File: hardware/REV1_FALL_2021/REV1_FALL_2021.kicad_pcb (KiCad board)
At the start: 2 copper layers, 146 x 133.4 mm, 38 parts, among them J101 Screw_Terminal_01x02, J102 Screw_Terminal_01x02, Q101 Q_NMOS_GDS, Q102 Q_NMOS_GDS, U1 Teensy3.6_All_Pins, U2 PA16165_Breakout, U201 TPS2113ADRBR, U3 MPL3115A2_Breakout, U301 TPS2113ADRBR, U4 BNO055_Breakout, U5 RFM69HCW_Breakout

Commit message: add logos and authors
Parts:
- added G***: LOGO, Olin_Rocketry:Olin_O, B.Cu at (97.9, 74.9)
- added G***: LOGO, Olin_Rocketry:Olin_Rocketry_Logo1, B.Cu at (100.2, 114.9)
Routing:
- net /E-MATCH_TRIGGER_2: track 0.00 -> 39.7 mm, vias 0 -> 1
- net GND: track 981.1 -> 982.8 mm
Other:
- board text added: "Ian Eykamp Marc Eftimie Charlie Babe Nov. 24, 2021 Pheonix IV Rev. 1"

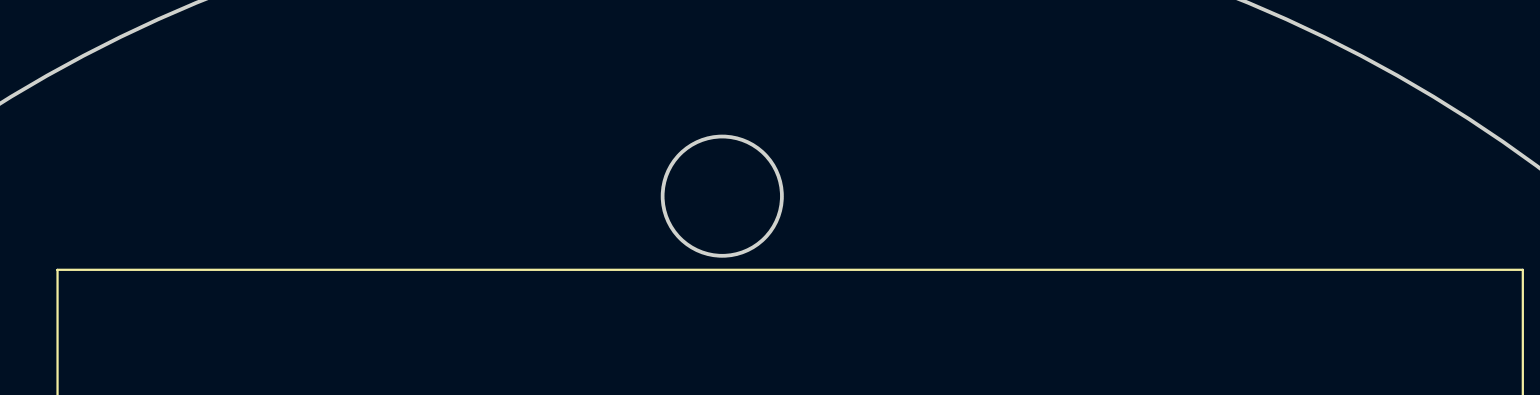
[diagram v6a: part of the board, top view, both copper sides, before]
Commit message: add positive and negative signs on battery terminals
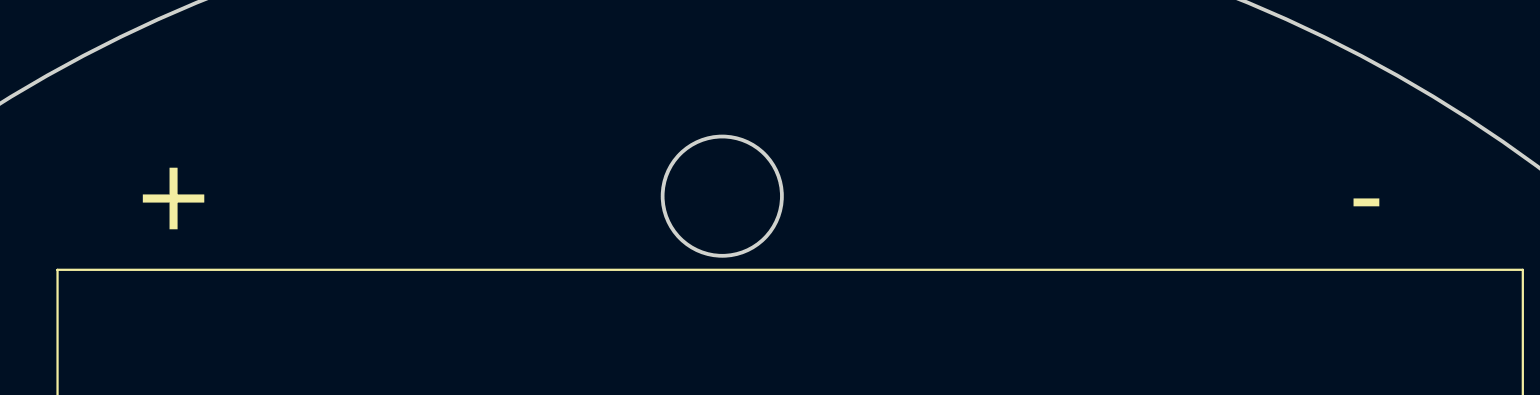
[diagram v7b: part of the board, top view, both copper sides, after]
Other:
- board text added: "+"
- board text added: "-"
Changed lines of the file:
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@@
   (general
     (thickness 1.6)
-    (drawings 6)
+    (drawings 8)
     (tracks 685)
     (zones 0)
@@
       (xy -13.7383 11.823811) (xy -13.641607 11.834288) (xy -13.637075 11.82514)) (layer B.SilkS) (width 0.01))
   )
+  (gr_text - (at 134.62 45.72) (layer F.SilkS)
+    (effects (font (size 3.81 3.81) (thickness 0.3)))
+  )
+  (gr_text + (at 71.12 45.72) (layer F.SilkS)
+    (effects (font (size 3.81 3.81) (thickness 0.3)))
+  )
   (gr_text "Ian Eykamp\nMarc Eftimie\nCharlie Babe\n\nNov. 24, 2021\nPheonix IV\nRev. 1" (at 129.286 145.923) (layer B.SilkS)

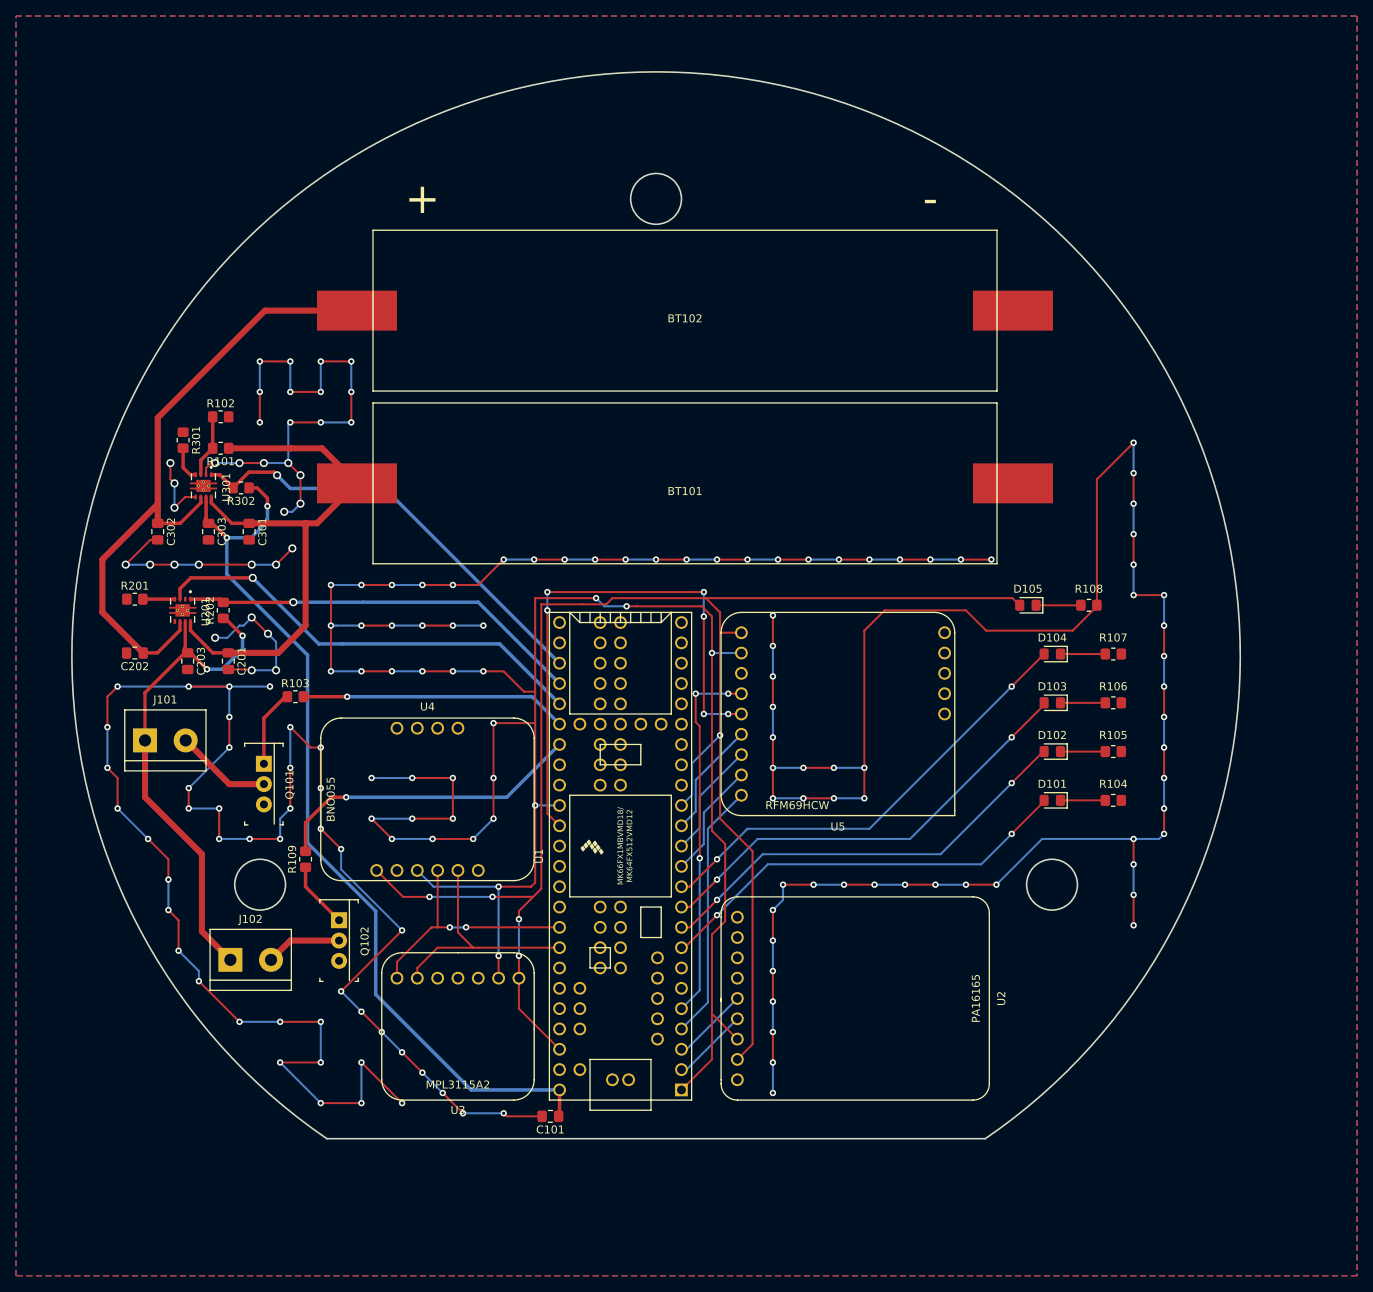
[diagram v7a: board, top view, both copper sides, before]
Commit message: Change footprint of TPS2113A to the TSSOP package
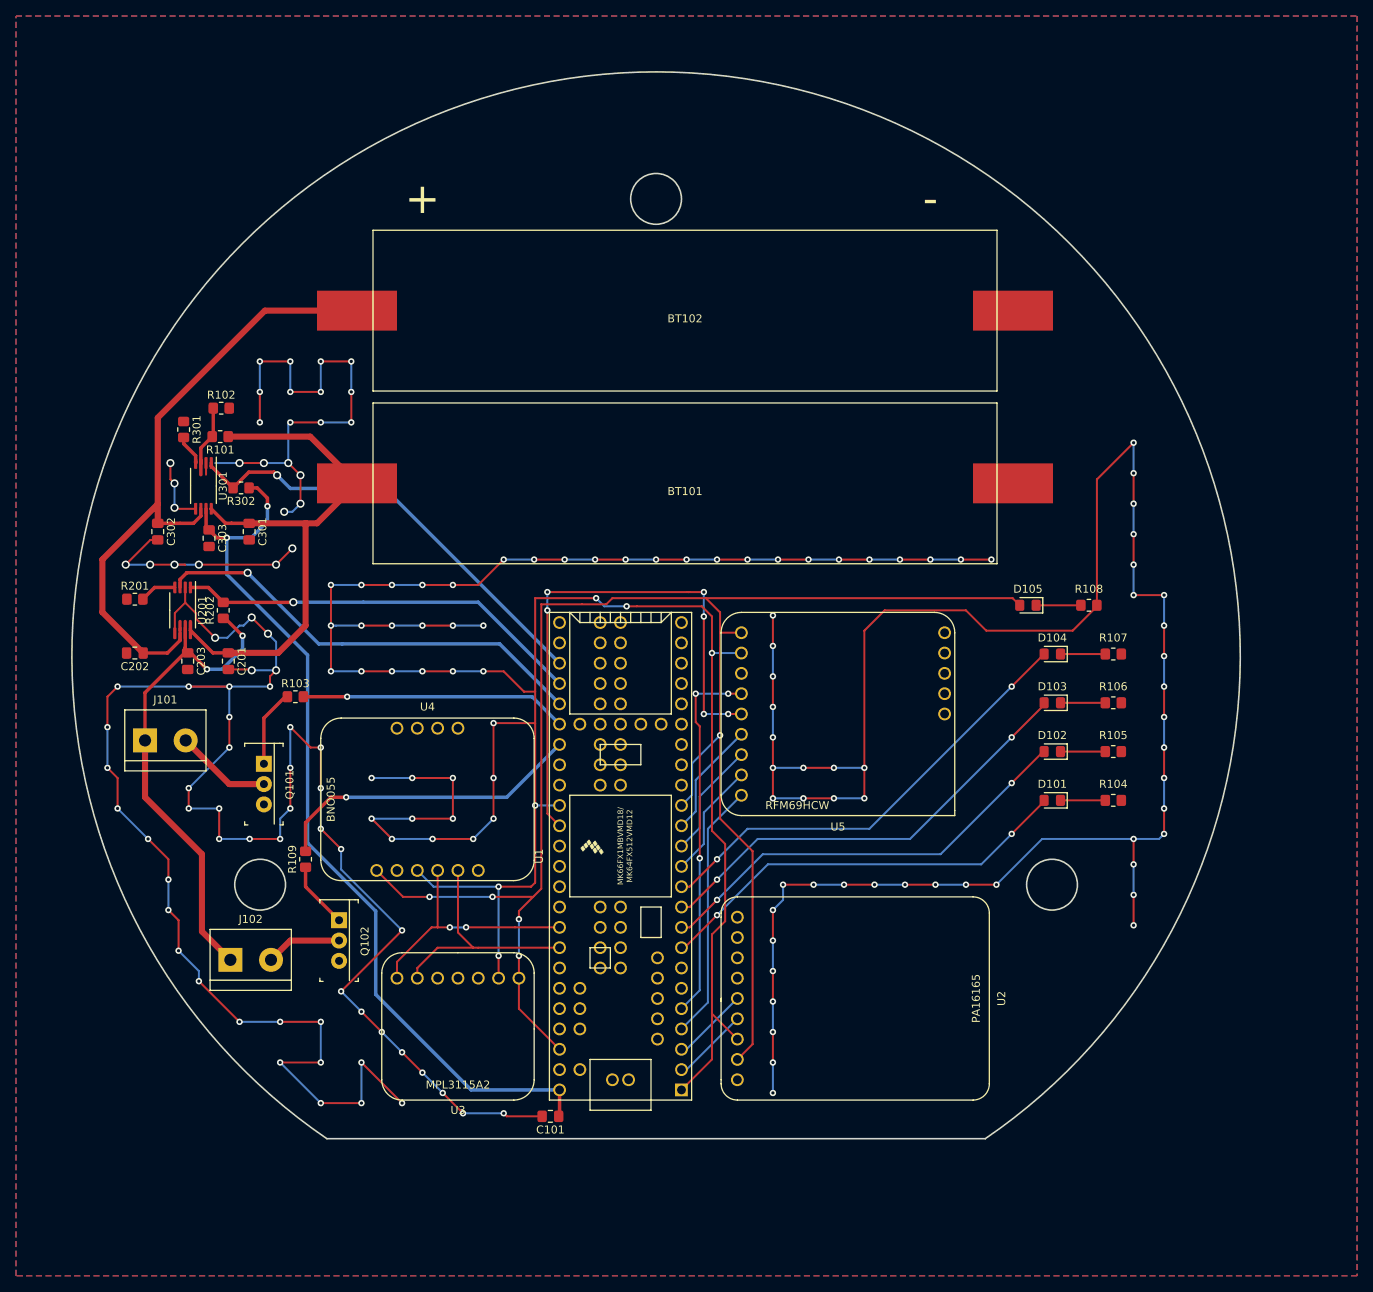
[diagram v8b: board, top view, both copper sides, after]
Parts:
- C201, C202, C301, C302: value C_0.1uF -> C_0.1u
- R201, R301: value R_250 -> R_270
- U201, U301: footprint footprints:TPS2113ADRBR -> Package_SO:TSSOP-8_4.4x3mm_P0.65mm
- moved R101 1.46 mm to (45.8, 75.4)
- moved R301 1.34 mm to (41.3, 74.5)
- moved R102 1.08 mm to (46.0, 71.9)
- moved C303 0.83 mm to (44.5, 88.1)
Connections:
- U1 pad 16: Net-(U1-Pad16) -> (no net)
- U1 pad 17: Net-(U1-Pad17) -> (no net)
- U1 pad 18: Net-(U1-Pad18) -> (no net)
- U1 pad 19: Net-(U1-Pad19) -> (no net)
- U1 pad 20: Net-(U1-Pad20) -> (no net)
- U1 pad 21: Net-(U1-Pad21) -> (no net)
- U1 pad 22: Net-(U1-Pad22) -> (no net)
- U1 pad 23: Net-(U1-Pad23) -> (no net)
- U1 pad 24: Net-(U1-Pad24) -> (no net)
- U1 pad 25: Net-(U1-Pad25) -> (no net)
- U1 pad 26: Net-(U1-Pad26) -> (no net)
- U1 pad 27: Net-(U1-Pad27) -> (no net)
- U1 pad 28: Net-(U1-Pad28) -> (no net)
- U1 pad 29: Net-(U1-Pad29) -> (no net)
- U1 pad 30: Net-(U1-Pad30) -> (no net)
- U1 pad 31: Net-(U1-Pad31) -> (no net)
- U1 pad 37: Net-(U1-Pad37) -> (no net)
- U1 pad 38: Net-(U1-Pad38) -> (no net)
- U1 pad 41: Net-(U1-Pad41) -> (no net)
- U1 pad 42: Net-(U1-Pad42) -> (no net)
- U1 pad 43: Net-(U1-Pad43) -> (no net)
- U1 pad 44: Net-(U1-Pad44) -> (no net)
- U1 pad 47: Net-(U1-Pad47) -> (no net)
- U1 pad 48: Net-(U1-Pad48) -> (no net)
- U1 pad 49: Net-(U1-Pad49) -> (no net)
- U1 pad 50: Net-(U1-Pad50) -> (no net)
- U1 pad 52: Net-(U1-Pad52) -> (no net)
- U1 pad 54: Net-(U1-Pad54) -> (no net)
- U1 pad 55: Net-(U1-Pad55) -> (no net)
- U1 pad 56: Net-(U1-Pad56) -> (no net)
- U1 pad 57: Net-(U1-Pad57) -> (no net)
- U1 pad 58: Net-(U1-Pad58) -> (no net)
- U1 pad 59: Net-(U1-Pad59) -> (no net)
- U1 pad 6: Net-(U1-Pad6) -> (no net)
- U1 pad 60: Net-(U1-Pad60) -> (no net)
- U1 pad 61: Net-(U1-Pad61) -> (no net)
- U1 pad 62: Net-(U1-Pad62) -> (no net)
- U1 pad 63: Net-(U1-Pad63) -> (no net)
- U1 pad 64: Net-(U1-Pad64) -> (no net)
- U1 pad 65: Net-(U1-Pad65) -> (no net)
- U1 pad 66: Net-(U1-Pad66) -> (no net)
- U1 pad 67: Net-(U1-Pad67) -> (no net)
- U1 pad 68: Net-(U1-Pad68) -> (no net)
- U1 pad 69: Net-(U1-Pad69) -> (no net)
- U1 pad 7: Net-(U1-Pad7) -> (no net)
- U1 pad 70: Net-(U1-Pad70) -> (no net)
- U1 pad 71: Net-(U1-Pad71) -> (no net)
- U1 pad 72: Net-(U1-Pad72) -> (no net)
- U1 pad 73: Net-(U1-Pad73) -> (no net)
- U1 pad 74: Net-(U1-Pad74) -> (no net)
- U1 pad 75: Net-(U1-Pad75) -> (no net)
- U1 pad 76: Net-(U1-Pad76) -> (no net)
- U1 pad 77: Net-(U1-Pad77) -> (no net)
- U1 pad 78: Net-(U1-Pad78) -> (no net)
- U1 pad 79: Net-(U1-Pad79) -> (no net)
- U1 pad 80: Net-(U1-Pad80) -> (no net)
- U1 pad 81: Net-(U1-Pad81) -> (no net)
- U1 pad 82: Net-(U1-Pad82) -> (no net)
- U1 pad 83: Net-(U1-Pad83) -> (no net)
- U1 pad 84: Net-(U1-Pad84) -> (no net)
- U1 pad 85: Net-(U1-Pad85) -> (no net)
- U1 pad 86: Net-(U1-Pad86) -> (no net)
- U1 pad 87: Net-(U1-Pad87) -> (no net)
- U1 pad 88: Net-(U1-Pad88) -> (no net)
- U2 pad 1: Net-(U2-Pad1) -> (no net)
- U2 pad 2: Net-(U2-Pad2) -> (no net)
- U2 pad 3: Net-(U2-Pad3) -> (no net)
- U2 pad 4: Net-(U2-Pad4) -> (no net)
- U2 pad 9: Net-(U2-Pad9) -> (no net)
- U3 pad 3: Net-(U3-Pad3) -> (no net)
- U3 pad 4: Net-(U3-Pad4) -> (no net)
- U3 pad 5: Net-(U3-Pad5) -> (no net)
- U4 pad 10: Net-(U4-Pad10) -> (no net)
- U4 pad 2: Net-(U4-Pad2) -> (no net)
- U4 pad 6: Net-(U4-Pad6) -> (no net)
- U4 pad 7: Net-(U4-Pad7) -> (no net)
- U4 pad 8: Net-(U4-Pad8) -> (no net)
- U4 pad 9: Net-(U4-Pad9) -> (no net)
- U5 pad 10: Net-(U5-Pad10) -> (no net)
- U5 pad 11: Net-(U5-Pad11) -> (no net)
- U5 pad 12: Net-(U5-Pad12) -> (no net)
- U5 pad 13: Net-(U5-Pad13) -> (no net)
- U5 pad 14: Net-(U5-Pad14) -> (no net)
- U5 pad 3: Net-(U5-Pad3) -> (no net)
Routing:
- net GND: track 982.8 -> 996.9 mm, vias 178 -> 176
- net /TPS2113A for Teensy power/VSNS: track 7.85 -> 9.31 mm
- net /V_TEENSY: track 114.4 -> 113.2 mm
- net /TPS_1_STAT: track 54.9 -> 55.8 mm
- net Net-(R201-Pad2): track 4.00 -> 4.60 mm
- net /TPS_2_STAT: track 50.5 -> 51.1 mm
